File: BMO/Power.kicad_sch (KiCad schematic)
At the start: 58 parts, among them J2 USB_C_Receptacle_USB2.0_16P, J3 Conn_01x03_Pin, J7 Conn_01x02, Q1 DMP1045U-7, U2 MMDT2907A-7-F, U3 USBLC6-2SC6, U4 BQ27220YZFR, U5 BQ25895RTW, U6 AP2112K-3.3, U7 TPS61023DRLR

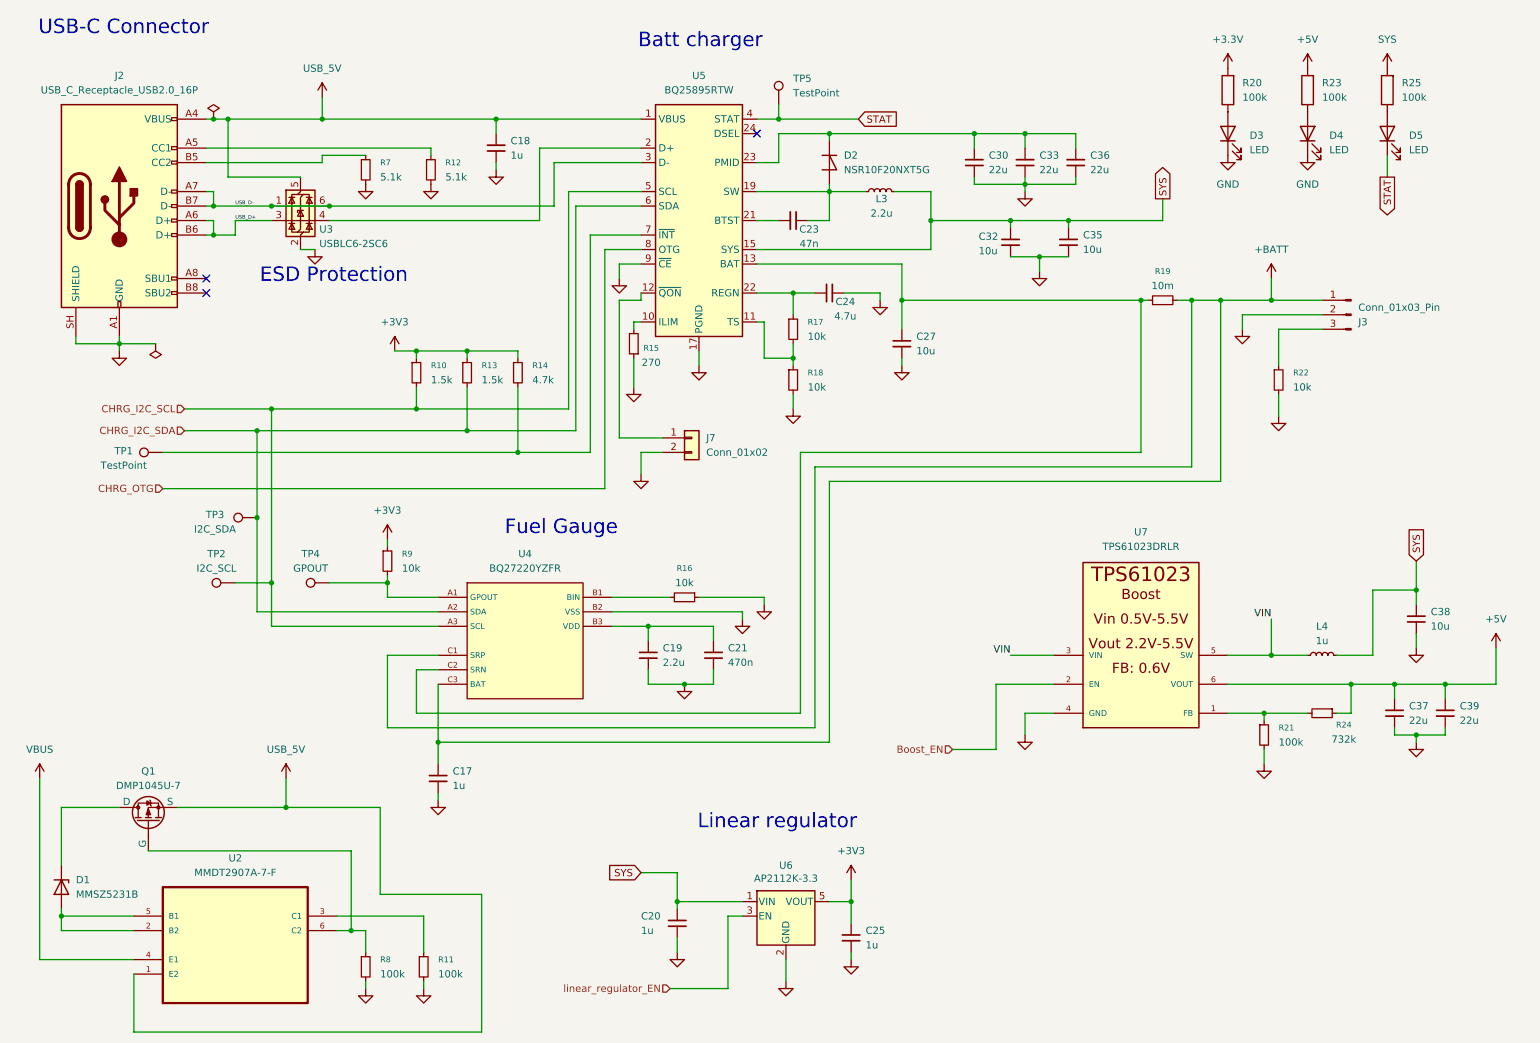
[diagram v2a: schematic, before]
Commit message: changed the charger to BQ25896RTW and updated the shematic
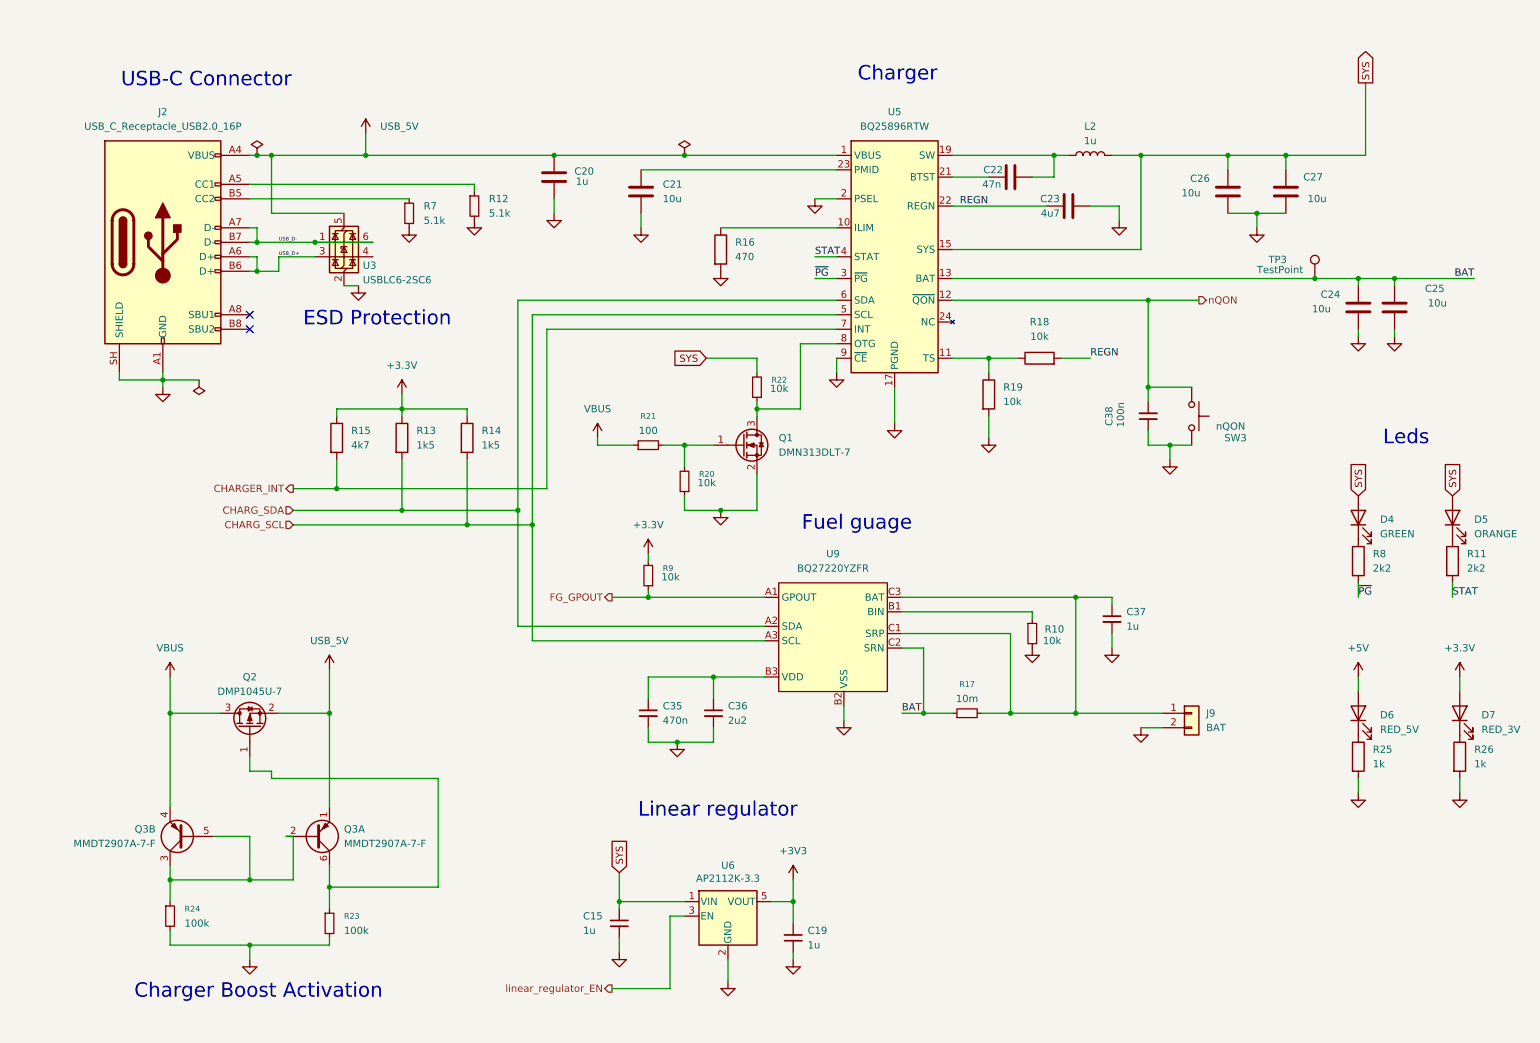
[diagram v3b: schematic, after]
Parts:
- removed C17, C18, C20, C25: 1u, Capacitor_SMD:C_0402_1005Metric, symbol Device:C_Small
- removed C21: 470n, Capacitor_SMD:C_0603_1608Metric, symbol Device:C_Small
- removed C23: 47n, Capacitor_SMD:C_0603_1608Metric, symbol Device:C_Small
- removed C24: 4.7u, Capacitor_SMD:C_0603_1608Metric, symbol Device:C_Small
- removed C27: 10u, Capacitor_SMD:C_0603_1608Metric, symbol Device:C_Small
- removed C30, C33, C39: 22u, Capacitor_SMD:C_1210_3225Metric, symbol Device:C_Small
- removed C32: 10u, Capacitor_SMD:C_0402_1005Metric, symbol Device:C_Small
- removed D1: MMSZ5231B, Diode_SMD:D_SOD-123, symbol Device:D_Zener
- removed D2: NSR10F20NXT5G, Diode_SMD:D_0603_1608Metric, symbol Device:D_Shockley
- removed D3, D4, D5: LED, symbol Kicad:LED
- removed J3: Conn_01x03_Pin, Connector_JST:JST_XH_B3B-XH-AM_1x03_P2.50mm_Vertical, symbol Connector:Conn_01x03_Pin
- removed J7: Conn_01x02, Connector_JST:JST_GH_SM02B-GHS-TB_1x02-1MP_P1.25mm_Horizontal, symbol Connector_Generic:Conn_01x02
- removed L3: 2.2u, Inductor_SMD:L_0603_1608Metric, symbol Device:L_Small
- removed L4: 1u, Inductor_SMD:L_0805_2012Metric, symbol Device:L_Small
- removed Q1: DMP1045U-7, Package_TO_SOT_SMD:SOT-23, symbol Simulation_SPICE:PMOS
- removed R11, R8: 100k, Resistor_SMD:R_0603_1608Metric, symbol Device:R_Small
- removed R13: 1.5k, Resistor_SMD:R_0201_0603Metric, symbol Device:R_Small
- removed R14: 4.7k, Resistor_SMD:R_0201_0603Metric, symbol Device:R_Small
- removed R15: 270, Resistor_SMD:R_0201_0603Metric, symbol Device:R_Small
- removed R16, R18: 10k, Resistor_SMD:R_0603_1608Metric, symbol Device:R_Small
- removed R19: 10m, Resistor_SMD:R_0603_1608Metric, symbol Device:R_Small
- removed R20, R23, R25: 100k, symbol Kicad:R
- removed TP1, TP5: TestPoint, symbol Connector:TestPoint
- removed TP2: I2C_SCL, symbol Connector:TestPoint
- removed TP4: GPOUT, symbol Connector:TestPoint
- removed U2: MMDT2907A-7-F, MMDT2907A-7-F:SOT65P210X110-6N, symbol jlcpcb_symbol:MMDT2907A-7-F
- removed U4: BQ27220YZFR, BQ27220:DSBGA-9_L1.7-W1.6-R3-C3-P0.50-BL, symbol jlcpcb_symbol:BQ27220YZFR
- removed U5: BQ25895RTW, Package_DFN_QFN:Texas_RTW_WQFN-24-1EP_4x4mm_P0.5mm_EP2.7x2.7mm_ThermalVias, symbol Battery_Management:BQ25895RTW
- removed U7: TPS61023DRLR, TPS61023DRLR:SOT563-ORI, symbol jlcpcb_symbol:TPS61023DRLR
- added C15: 1u, Capacitor_SMD:C_0402_1005Metric, symbol Device:C_Small
- added C20: 1u, Capacitor_SMD:C_0402_1005Metric, symbol Device:C
- added C21, C24, C25, C26, C27: 10u, Capacitor_SMD:C_0603_1608Metric, symbol Device:C
- added C22: 47n, Capacitor_SMD:C_0402_1005Metric, symbol Device:C
- added C23: 4u7, Capacitor_SMD:C_0402_1005Metric, symbol Device:C
- added D4: GREEN, LED_SMD:LED_0603_1608Metric, symbol Device:LED
- added D5: ORANGE, LED_SMD:LED_0603_1608Metric, symbol Device:LED
- added D6: RED_5V, LED_SMD:LED_0603_1608Metric, symbol Device:LED
- added D7: RED_3V, LED_SMD:LED_0603_1608Metric, symbol Device:LED
- added J9: BAT, Connector_JST:JST_GH_SM02B-GHS-TB_1x02-1MP_P1.25mm_Horizontal, symbol Connector_Generic:Conn_01x02
- added L2: 1u, Inductor_SMD:L_1008_2520Metric, symbol Device:L
- added Q1: DMN313DLT-7, Package_TO_SOT_SMD:SOT-523, symbol Transistor_FET:DMN3150L
- added Q2: DMP1045U-7, Package_TO_SOT_SMD:SOT-23, symbol Transistor_FET:DMP3099L
- added Q3: MMDT2907A-7-F, Package_TO_SOT_SMD:SOT-363_SC-70-6, symbol Transistor_BJT:MMDT3906
- added R11, R8: 2k2, Resistor_SMD:R_0402_1005Metric, symbol Device:R
- added R13, R14: 1k5, Resistor_SMD:R_0402_1005Metric, symbol Device:R
- added R15: 4k7, Resistor_SMD:R_0402_1005Metric, symbol Device:R
- added R16: 470, Resistor_SMD:R_0402_1005Metric, symbol Device:R
- added R18, R19: 10k, Resistor_SMD:R_0402_1005Metric, symbol Device:R
- added R20: 10k, Resistor_SMD:R_0402_1005Metric, symbol Device:R_Small
- added R23: 100k, Resistor_SMD:R_0402_1005Metric, symbol Device:R_Small
- added R25, R26: 1k, Resistor_SMD:R_0402_1005Metric, symbol Device:R
- added SW3: nQON, Button_Switch_SMD:SW_Push_1P1T_NO_CK_KMR2, symbol Switch:SW_Push
- added U5: BQ25896RTW, Package_DFN_QFN:Texas_RTW_WQFN-24-1EP_4x4mm_P0.5mm_EP2.7x2.7mm, symbol power_lib:BQ25896RTW
- added U9: BQ27220YZFR, Package_BGA:Texas_DSBGA-9_1.62x1.58mm_Layout3x3_P0.5mm, symbol power_lib:BQ27220YZFR
- C19: value 2.2u -> 1u; footprint Capacitor_SMD:C_0603_1608Metric -> Capacitor_SMD:C_0402_1005Metric; JLCPCB Part # C23630 -> C52923
- C35: value 10u -> 470n; JLCPCB Part # C15525 -> C162162
- C36: value 22u -> 2u2; footprint Capacitor_SMD:C_1210_3225Metric -> Capacitor_SMD:C_0402_1005Metric; JLCPCB Part # C52306 -> C72203
- C37: value 22u -> 1u; footprint Capacitor_SMD:C_1210_3225Metric -> Capacitor_SMD:C_0402_1005Metric; JLCPCB Part # C52306 -> C52923
- C38: value 10u -> 100n; footprint Capacitor_SMD:C_0603_1608Metric -> Capacitor_SMD:C_0402_1005Metric; JLCPCB Part # C96446 -> C1525
- R10: value 1.5k -> 10k; footprint Resistor_SMD:R_0201_0603Metric -> Resistor_SMD:R_0402_1005Metric; JLCPCB Part # C22843 -> C25744
- R17: value 10k -> 10m; footprint Resistor_SMD:R_0603_1608Metric -> Resistor_SMD:R_2512_6332Metric; JLCPCB Part # C25804 -> C105142
- R21: value 100k -> 100; footprint Resistor_SMD:R_0603_1608Metric -> Resistor_SMD:R_0402_1005Metric; JLCPCB Part # C25803 -> C25138
- R22, R9: footprint Resistor_SMD:R_0603_1608Metric -> Resistor_SMD:R_0402_1005Metric; JLCPCB Part # C25804 -> C25744
- R24: value 732k -> 100k; footprint Resistor_SMD:R_0603_1608Metric -> Resistor_SMD:R_0402_1005Metric; JLCPCB Part # C23239 -> C25741
- TP3: value I2C_SDA -> TestPoint; footprint BQ27220:DSBGA-9_L1.7-W1.6-R3-C3-P0.50-BL -> TestPoint:TestPoint_Pad_D2.0mm
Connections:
- net CHRG_I2C_SCL is gone; now on net GND: R10.2
- net CHRG_I2C_SDA is gone; now on net BAT: TP3.1
- net +3.3V: now also R9.2, D7.2 (A), R13.1, R14.1, R15.1
- net +3V3: now also C19.1; no longer R10.1, R9.1
- net +5V: now also D6.2 (A); no longer C37.1, R24.1
- net GND: now also C38.1, R24.2, C15.2, C20.2, C21.2, C23.2, C24.2, C25.2, C26.2, C27.2, J9.2 (Pin_2), Q1.2 (S), R16.2, R19.2, R20.1, R23.2, R25.2, R26.2, SW3.2, U5.17 (PGND), U5.18 (PGND), U5.2 (PSEL), U5.9 (~{CE}), U9.B2 (VSS); no longer C38.2, R21.2, R22.2
- net STAT: now also R11.2, U5.4 (STAT)
- net SYS: now also R22.2, C15.1, C26.1, C27.1, D4.2 (A), D5.2 (A), L2.2, U5.15 (SYS), U5.16 (SYS); no longer C35.1, C38.1
- net USB_5V: now also C20.1, Q2.2 (S), Q3.1 (E1), U5.1 (VBUS)
- net VBUS: now also R21.1, Q2.3 (D), Q3.4 (E2)
- net at C36.1: now also C35.1, U9.B3 (VDD)
- net at R17.2: now also C37.1, J9.1 (Pin_1), U9.C1 (SRP), U9.C3 (BAT)
- net BAT: now reaches R17.1
- net BAT: now also C24.1, C25.1, U5.13 (BAT), U5.14 (BAT), U9.C2 (SRN)
- net at R22.1: now also Q1.3 (D), U5.8 (OTG)
- new net: D6.1 (K), R25.1
- new net: D7.1 (K), R26.1
- new net: Q3.2 (B1), Q3.3 (C2), Q3.5 (B2), R24.1
- new net: Q2.1 (G), Q3.6 (C1), R23.1
- new net: R10.1, U9.B1 (BIN)
- new net: D5.1 (K), R11.1
- new net: R18.1, R19.1, U5.11 (TS)
- new net: D4.1 (K), R8.1
- new net: R16.1, U5.10 (ILIM)
- new net: C22.2, L2.1, U5.19 (SW), U5.20 (SW)
- new net: C22.1, U5.21 (BTST)
- new net: C21.1, U5.23 (PMID)
- new net: Q1.1 (G), R20.2, R21.2
- new net CHARGER_INT: R15.2, U5.7 (INT)
- new net CHARG_SCL: R14.2, U5.5 (SCL), U9.A3 (SCL)
- new net CHARG_SDA: R13.2, U5.6 (SDA), U9.A2 (SDA)
- new net FG_GPOUT: R9.1, U9.A1 (GPOUT)
- new net REGN: C23.1, R18.2, U5.22 (REGN)
- new net nQON: C38.2, SW3.1, U5.12 (~{QON})
- new net ~{PG}: R8.2, U5.3 (~{PG})
- no-connect marks 3 -> 2
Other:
- note added: "Charger"
- note added: "Charger Boost Activation"
- note added: "Fuel guage"
- note added: "Leds"
- note removed: "Batt charger"
- note removed: "Fuel Gauge"

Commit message: Update PCB modifications
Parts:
- added JP1, JP2, JP3: SolderJumper_2_Open, Jumper:SolderJumper-2_P1.3mm_Open_TrianglePad1.0x1.5mm, symbol Jumper:SolderJumper_2_Open
- added R21: 10k, Resistor_SMD:R_0402_1005Metric, symbol Device:R
- added TP1, TP2, TP3, TP4, TP5, TP6, TP7, TP9: TestPoint, TestPoint:TestPoint_Pad_D1.5mm, symbol Connector:TestPoint
- J10: renamed from J9; footprint Connector_JST:JST_GH_SM02B-GHS-TB_1x02-1MP_P1.25mm_Horizontal -> TerminalBlock_Phoenix:TerminalBlock_Phoenix_MKDS-1,5-2-5.08_1x02_P5.08mm_Horizontal
- U4: renamed from U6; JLCPCB Part # (none) -> C51118
- renumbered C20 to C22, C15 to C23, C21 to C24, C35 to C25, C36 to C26, C19 to C27, C22 to C28, C23 to C29, C37 to C30, C38 to C31, C26 to C32, C27 to C33, C24 to C34, C25 to C35, D4 to D2, D6 to D3, D5 to D4, D7 to D5, J2 to J9, Q3 to Q1, Q1 to Q3, R23 to R10, R15 to R11, R13 to R12, R7 to R13, R12 to R15, R21 to R16, R9 to R17, R20 to R18, R16 to R19, R22 to R20, R17 to R22, R19 to R23, R10 to R24, R18 to R25, R8 to R26, R25 to R27, R11 to R28, R26 to R29, R24 to R9, TP3 to TP8, U9 to U5, U5 to U6
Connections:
- net +3V3 is gone; now on net +3.3V: C27.1, U4.5 (VOUT)
- net +3.3V: now also TP7.1
- net +5V: now also Q1.1 (E1), Q2.2 (S), JP2.1 (A), TP5.1
- net CHARGER_INT: now also TP3.1
- net CHARG_SCL: now also TP2.1
- net CHARG_SDA: now also TP4.1
- net GND: now also U6.25 (PAD), R21.1, TP1.1; no longer U6.2 (PSEL)
- net SYS: now also JP3.2 (B), TP9.1; no longer C23.1, U4.1 (VIN)
- net USB_D-: no longer U3.6 (I/O1)
- net VBUS: now also JP1.2 (B), TP6.1
- net USB_5V: no longer names the net of J9.A4 (VBUS), J9.A9 (VBUS), J9.B4 (VBUS), J9.B9 (VBUS), U3.5 (VBUS)
- net USB_5V: now also JP1.1 (A); no longer C22.1, Q1.1 (E1), Q2.2 (S), U6.1 (VBUS)
- new net: C23.1, JP3.1 (A), U4.1 (VIN)
- new net: R21.2, U6.2 (PSEL)
- new net: C22.1, JP2.2 (B), U6.1 (VBUS)
- no-connect marks 2 -> 4
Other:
- note added: "Remplacer par TVS (facultatif)"

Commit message: Schéma prêt pour le PCB
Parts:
- added D7: BAT54WS, Diode_SMD:D_SOD-323, symbol Device:D_Schottky
- C22, C23, C27, C30: LCSC (none) -> C52923
- C24, C32, C33, C34, C35: JLCPCB Part # C70225 -> C96446; LCSC (none) -> C96446
- C25: JLCPCB Part # C162162 -> C88946; LCSC (none) -> C88946
- C26: JLCPCB Part # C72203 -> C12530; LCSC (none) -> C12530
- C28: JLCPCB Part # C82219 -> C77012; LCSC (none) -> C77012
- C29: footprint Capacitor_SMD:C_0402_1005Metric -> Capacitor_SMD:C_0603_1608Metric; JLCPCB Part # C318563 -> C19666; LCSC (none) -> C19666
- C31: LCSC (none) -> C1525
- D2: JLCPCB Part # C99289 -> C12624; LCSC (none) -> C12624
- D3, D5: LCSC (none) -> C2286
- D4: LCSC (none) -> C84269
- J10: JLCPCB Part # C54769875 -> C480516; LCSC (none) -> C480516
- J9: JLCPCB Part # C2765186 -> C3020560; LCSC (none) -> C3020560
- L2: footprint Inductor_SMD:L_1008_2520Metric -> Inductor_SMD:L_APV_ANR4020; JLCPCB Part # C167447 -> C7497071; LCSC (none) -> C7497071
- Q1: LCSC (none) -> C460232
- Q2: LCSC (none) -> C177033
- Q3: LCSC (none) -> C155524
- R10, R9: LCSC (none) -> C25741
- R11: LCSC (none) -> C25900
- R12, R14: LCSC (none) -> C25867
- R13, R15: LCSC (none) -> C23186
- R16: JLCPCB Part # C25138 -> C25076; LCSC (none) -> C25076
- R17, R18, R20, R21, R23, R24, R25: LCSC (none) -> C25744
- R19: LCSC (none) -> C25117
- R22: JLCPCB Part # C105142 -> C105366; LCSC (none) -> C105366
- R26, R28: LCSC (none) -> C25879
- R27, R29: LCSC (none) -> C11702
- SW3: LCSC (none) -> C72443
- U3: LCSC (none) -> C7519
- U4: JLCPCB Part # C51118 -> C51118; LCSC (none) -> C51118
- U5: LCSC (none) -> C528617
- U6: footprint Package_DFN_QFN:Texas_RTW_WQFN-24-1EP_4x4mm_P0.5mm_EP2.7x2.7mm -> Package_DFN_QFN:Texas_RTW_WQFN-24-1EP_4x4mm_P0.5mm_EP2.7x2.7mm_ThermalVias; LCSC (none) -> C181475
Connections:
- net nQON: now also D7.1 (K)
- new net PWR_Bouton: D7.2 (A)

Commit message: pcb(layout): finalize placement post-review and initiate routing
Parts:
- removed D7: BAT54WS, Diode_SMD:D_SOD-323, symbol Device:D_Schottky
- removed J10: BAT, TerminalBlock_Phoenix:TerminalBlock_Phoenix_MKDS-1,5-2-5.08_1x02_P5.08mm_Horizontal, symbol Connector_Generic:Conn_01x02
- added J11: BAT, Connector_JST:JST_XH_S2B-XH-A-1_1x02_P2.50mm_Horizontal, symbol Connector_Generic:Conn_01x02
- renumbered C22 to C24, C23 to C25, C24 to C26, C25 to C27, C26 to C28, C27 to C29, C28 to C30, C29 to C31, C30 to C32, C31 to C33, C32 to C34, C33 to C35, C34 to C36, C35 to C37, J9 to J10, R9 to R10, R10 to R11, R11 to R12, R12 to R13, R13 to R14, R14 to R15, R15 to R16, R16 to R17, R17 to R18, R18 to R19, R19 to R20, R20 to R21, R21 to R22, R22 to R23, R23 to R24, R24 to R25, R25 to R26, R26 to R27, R27 to R28, R28 to R29, R29 to R30, U3 to U4, U4 to U5, U5 to U6, U6 to U7
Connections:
- net nQON is gone; now on net PWR_Bouton: C33.2, SW3.1, U7.12 (~{QON})
- net GND: now also J11.2 (Pin_2)
- net at C32.1, R23.2, U6.C1 (SRP)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: now also J11.1 (Pin_1)

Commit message: Mise à jour des fichiers PCB
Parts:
- added TP11: TestPoint, TestPoint:TestPoint_Pad_D1.5mm, symbol Connector:TestPoint
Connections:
- net at J10.A4 (VBUS), J10.A9 (VBUS), J10.B4 (VBUS)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: now also TP11.1
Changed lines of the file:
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@@
 	(wire
 		(pts
+			(xy 58.42 36.83) (xy 58.42 40.64)
+		)
+		(stroke
+			(width 0)
+			(type default)
+		)
+	)
+	(wire
+		(pts
 			(xy 81.28 82.55) (xy 81.28 85.09)
 		)
@@
 					(unit 1)
 				)
+			)
+		)
+	)
+	(symbol
+		(lib_id "Connector:TestPoint")
+		(at 58.42 36.83 0)
+		(unit 1)
+		(body_style 1)
+		(exclude_from_sim no)
+		(in_bom yes)
+		(on_board yes)
+		(in_pos_files yes)
+		(dnp no)
+		(fields_autoplaced yes)
+		(property "Reference" "TP11"
+			(at 63.5 36.8299 90)
+			(show_name no)
+			(do_not_autoplace no)
+			(effects
+				(font
+					(size 1.27 1.27)
+				)
+				(justify left)
+			)
+		)
+		(property "Value" "TestPoint"
+			(at 63.5 38.0999 90)
+			(hide yes)
+			(show_name no)
+			(do_not_autoplace no)
+			(effects
+				(font
+					(size 1.27 1.27)
+				)
+				(justify left)
+			)
+		)
+		(property "Footprint" "TestPoint:TestPoint_Pad_D1.5mm"
+			(at 58.42 41.91 0)
+			(hide yes)
+			(show_name no)
+			(do_not_autoplace no)
+			(effects
+				(font
+					(size 1.27 1.27)
+				)
+			)
+		)
+		(property "Datasheet" ""
+			(at 58.42 41.91 0)
+			(hide yes)
+			(show_name no)
+			(do_not_autoplace no)
+			(effects
+				(font
+					(size 1.27 1.27)
+				)
+			)
+		)
+		(property "Description" "test point"
+			(at 58.42 36.83 0)
+			(hide yes)
+			(show_name no)
+			(do_not_autoplace no)
+			(effects
+				(font
+					(size 1.27 1.27)
+				)
+			)
+		)
+		(pin "1"
+		)
+		(instances
+			(project "BMO"
+				(path "/509804e7-65e7-46e6-80ed-6cdb4037dc07/a118be83-9452-4230-9073-78ab810a1c4b"
+					(reference "TP11")
+					(unit 1)
+				)

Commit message: updated the shematic and routed the pcb
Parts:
- removed R13, R15: 1k5, Resistor_SMD:R_0402_1005Metric, symbol Device:R
